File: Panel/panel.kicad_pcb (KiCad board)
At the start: 4 copper layers, 70 x 116 mm, 150 parts, among them J1 Conn_01x03, U1 USB-C, U13 ESP32-C6-MINI-1-N4, U3 AHT20, U4 Tactile-Switch, U6 Light sensor, U7 Tactile-Switch, U8 Slide-Switch, U9 Battery-Spring

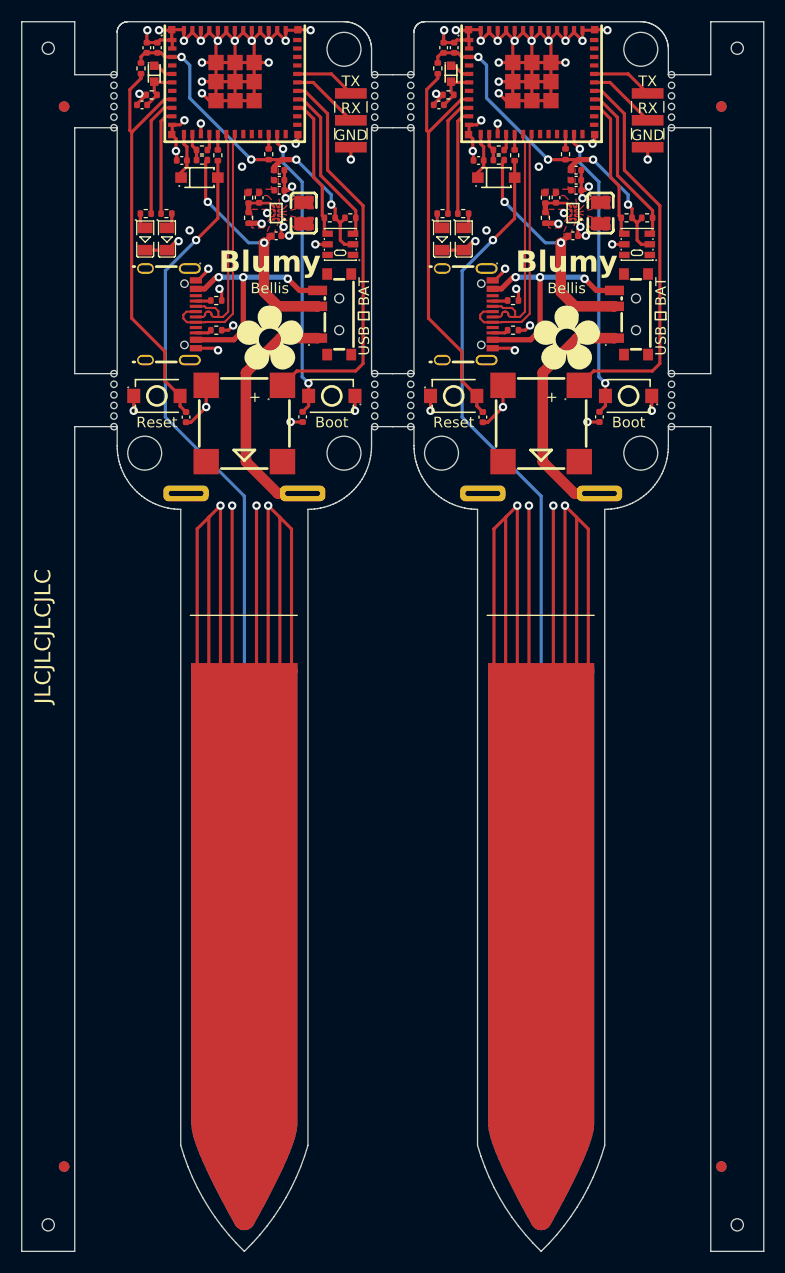
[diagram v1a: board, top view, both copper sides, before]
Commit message: Add missing tabs to blumy panel
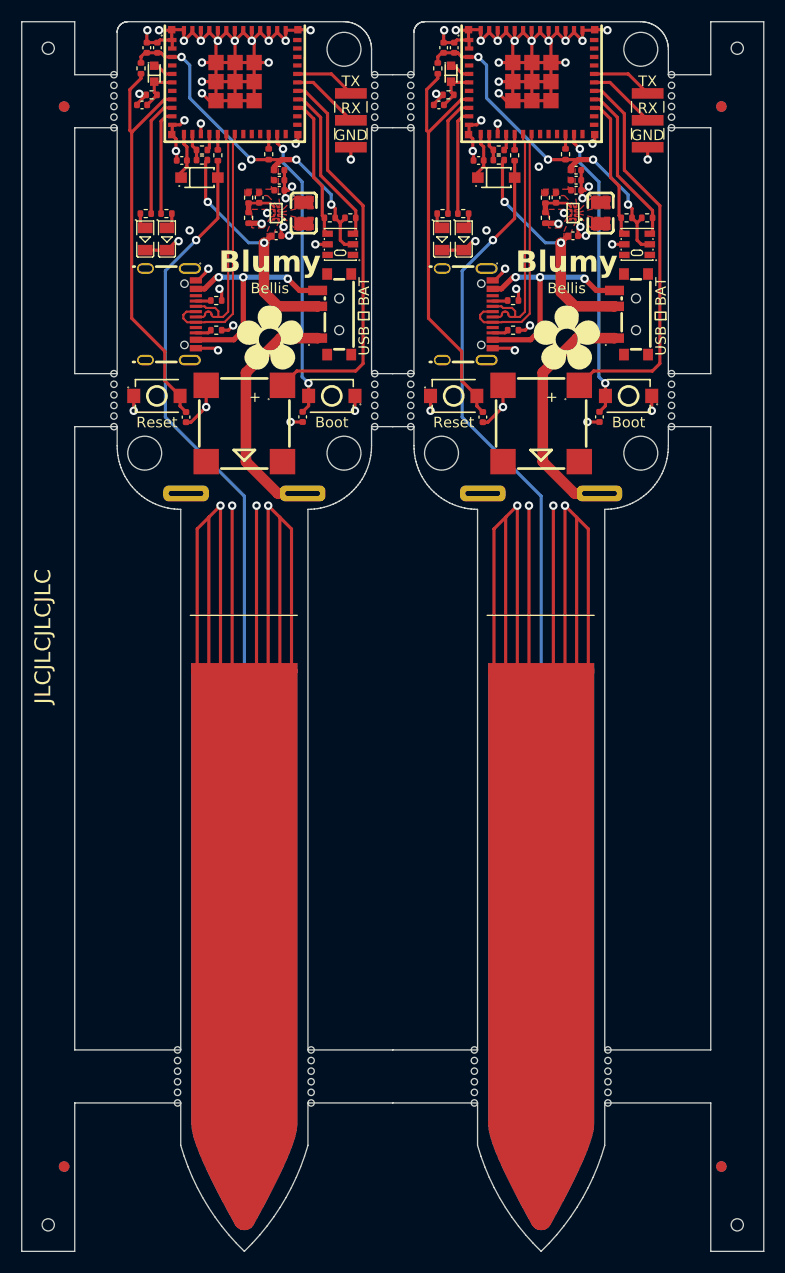
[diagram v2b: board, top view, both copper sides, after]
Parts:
- added KiKit_MB_10_1: NPTH, NPTH, F.Cu at (245.3, 117.0)
- added KiKit_MB_10_2: NPTH, NPTH, F.Cu at (245.3, 118.0)
- added KiKit_MB_10_3: NPTH, NPTH, F.Cu at (245.3, 119.0)
- added KiKit_MB_10_4: NPTH, NPTH, F.Cu at (245.3, 120.0)
- added KiKit_MB_10_5: NPTH, NPTH, F.Cu at (245.3, 121.0)
- added KiKit_MB_10_6: NPTH, NPTH, F.Cu at (245.3, 122.0)
- added KiKit_MB_11_1: NPTH, NPTH, F.Cu at (226.7, 58.2)
- added KiKit_MB_11_2: NPTH, NPTH, F.Cu at (226.7, 57.2)
- added KiKit_MB_11_3: NPTH, NPTH, F.Cu at (226.7, 56.2)
- added KiKit_MB_11_4: NPTH, NPTH, F.Cu at (226.7, 55.2)
- added KiKit_MB_11_5: NPTH, NPTH, F.Cu at (226.7, 54.2)
- added KiKit_MB_11_6: NPTH, NPTH, F.Cu at (226.7, 53.2)
- added KiKit_MB_12_1: NPTH, NPTH, F.Cu at (226.7, 30.0)
- added KiKit_MB_12_2: NPTH, NPTH, F.Cu at (226.7, 29.0)
- added KiKit_MB_12_3: NPTH, NPTH, F.Cu at (226.7, 28.0)
- added KiKit_MB_12_4: NPTH, NPTH, F.Cu at (226.7, 27.0)
- added KiKit_MB_12_5: NPTH, NPTH, F.Cu at (226.7, 26.0)
- added KiKit_MB_12_6: NPTH, NPTH, F.Cu at (226.7, 25.0)
- added KiKit_MB_9_1: NPTH, NPTH, F.Cu at (251.3, 25.0)
- added KiKit_MB_9_2: NPTH, NPTH, F.Cu at (251.3, 26.0)
- added KiKit_MB_9_3: NPTH, NPTH, F.Cu at (251.3, 27.0)
- added KiKit_MB_9_4: NPTH, NPTH, F.Cu at (251.3, 28.0)
- added KiKit_MB_9_5: NPTH, NPTH, F.Cu at (251.3, 29.0)
- added KiKit_MB_9_6: NPTH, NPTH, F.Cu at (251.3, 30.0)
- moved KiKit_MB_4_6 98.8 mm to (217.3, 122.0)
- moved KiKit_MB_4_5 96.8 mm to (217.3, 121.0)
- moved KiKit_MB_4_4 94.8 mm to (217.3, 120.0)
- moved KiKit_MB_4_3 92.9 mm to (217.3, 119.0)
- moved KiKit_MB_4_2 90.9 mm to (217.3, 118.0)
- moved KiKit_MB_4_1 89.0 mm to (217.3, 117.0)
- moved KiKit_MB_1_1 71.3 mm to (204.7, 122.0)
- moved KiKit_MB_1_2 69.3 mm to (204.7, 121.0)
- moved KiKit_MB_1_3 67.4 mm to (204.7, 120.0)
- moved KiKit_MB_1_4 65.5 mm to (204.7, 119.0)
- moved KiKit_MB_7_1 64.1 mm to (232.7, 122.0)
- moved KiKit_MB_7_2 64.1 mm to (232.7, 121.0)
- moved KiKit_MB_7_3 64.1 mm to (232.7, 120.0)
- moved KiKit_MB_7_4 64.1 mm to (232.7, 119.0)
- moved KiKit_MB_7_5 64.1 mm to (232.7, 118.0)
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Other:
- outline, holes or cut-outs redrawn
